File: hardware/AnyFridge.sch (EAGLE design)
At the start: 6 parts, among them U1 TSSP77038TT

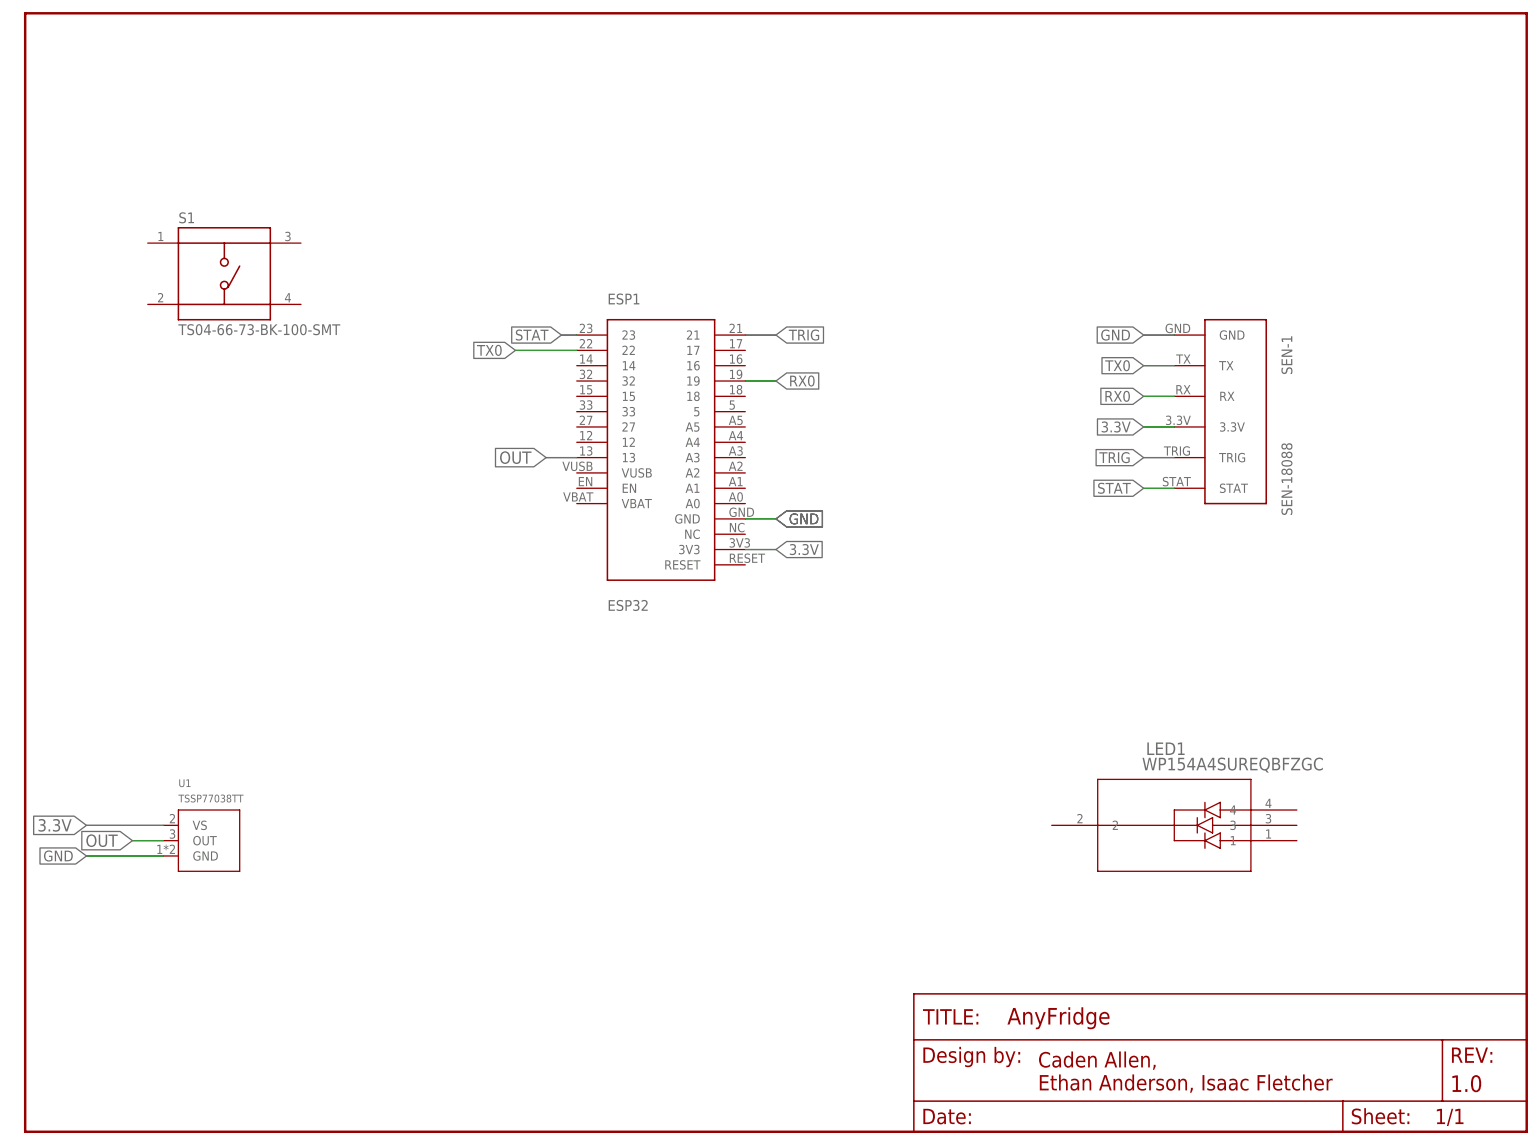
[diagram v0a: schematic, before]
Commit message: Wire LED + Button, change UART
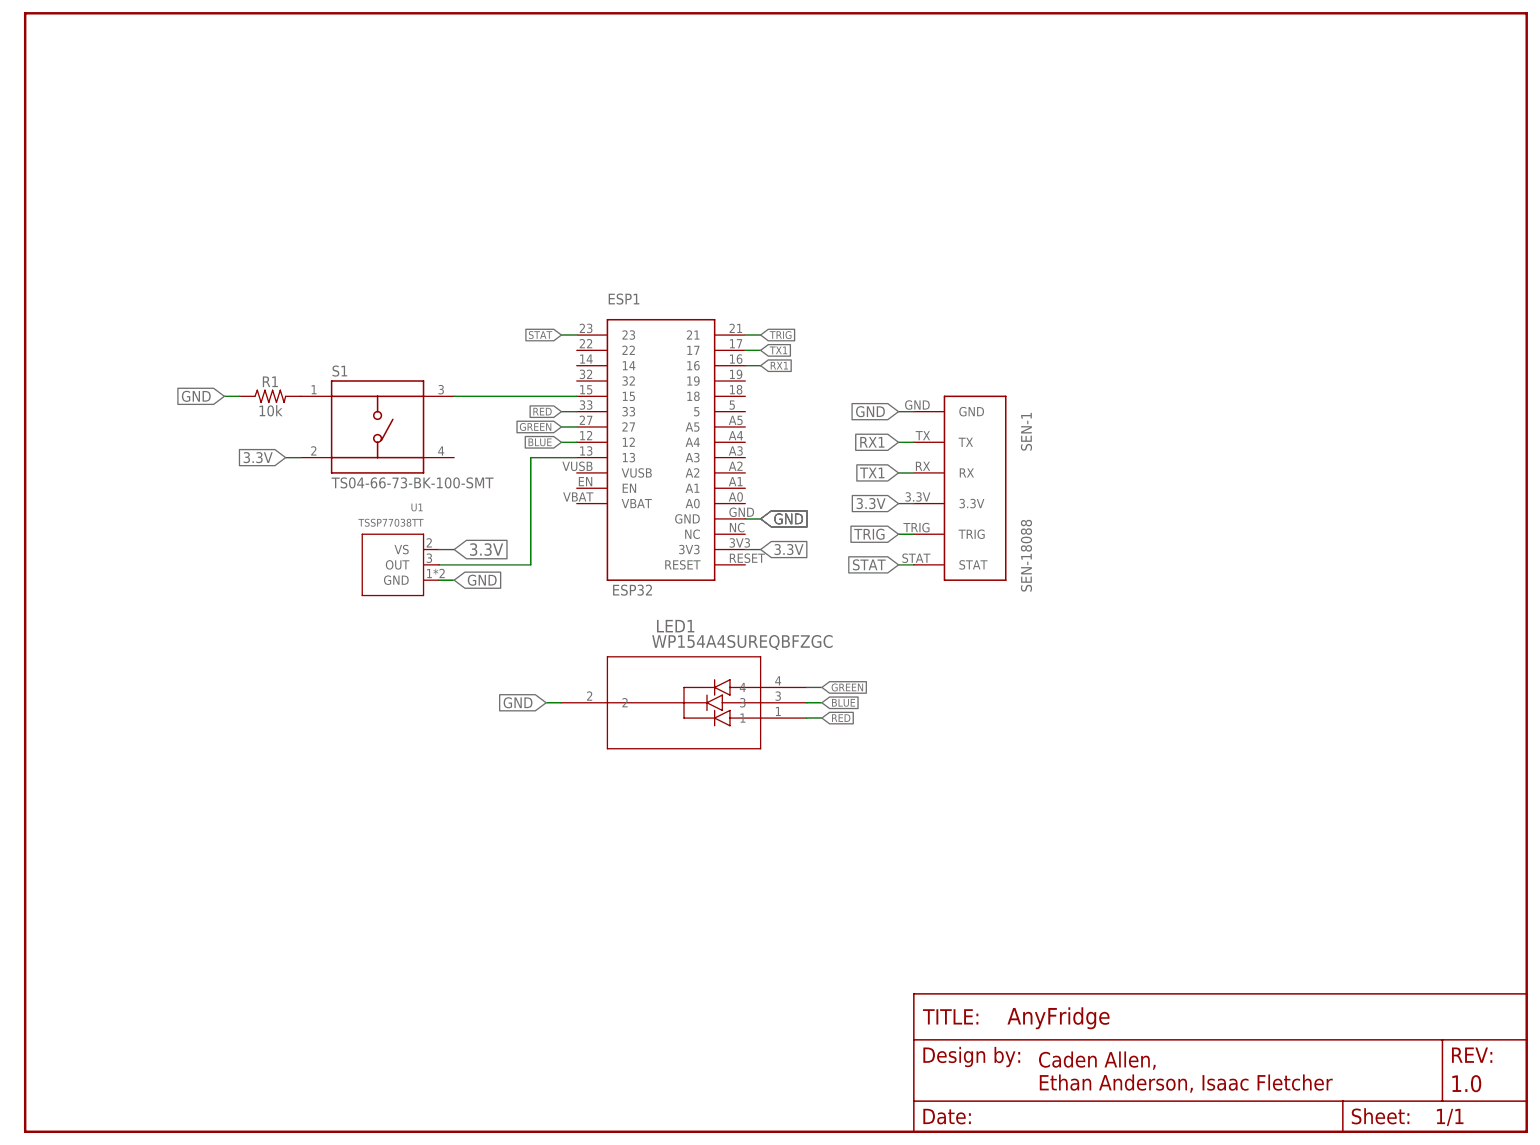
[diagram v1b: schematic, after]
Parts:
- added R1: 10k, SparkFun-Resistors:10KOHM-HORIZ-1/4W-1%
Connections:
- removed net RX0: ESP1.19, SEN-1.RX
- removed net TX0: ESP1.22, SEN-1.TX
- new net BLUE: ESP1.12, LED1.3
- new net BUTTON: ESP1.15, S1.3
- new net GREEN: ESP1.27, LED1.4
- new net N$1: R1.2, S1.1
- new net RED: ESP1.33, LED1.1
- new net RX1: ESP1.16, SEN-1.TX
- new net TX1: ESP1.17, SEN-1.RX
- net 3.3V: now also S1.2
- net GND: now also LED1.2, R1.1
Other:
- moved on the sheet: LED1, S1, SEN-1, U1

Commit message: Updated schematic
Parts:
- removed ESP1: ESP32, ESP32:ESP32
- removed LED1: WP154A4SUREQBFZGC, MISC-PARTS:WP154A4SUREQBFZGC
- removed S1: TS04-66-73-BK-100-SMT, MISC-PARTS:TS04-66-73-BK-100-SMT
- removed SEN-1: SEN-18088, SEN-18088:SEN-18088
- removed U1: TSSP77038TT, MISC-PARTS:TSSP77038TT
- added ESP: ESP32, ESP32:ESP32
- added LED: WP154A4SUREQBFZGC, MISC-PARTS:WP154A4SUREQBFZGC
- added SCANNER: SEN-18088, SEN-18088:SEN-18088
- added SENSOR: TSSP77038TT, MISC-PARTS:TSSP77038TT
- added SWITCH: TS04-66-73-BK-100-SMT, MISC-PARTS:TS04-66-73-BK-100-SMT
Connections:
- net 3.3V: now also ESP.3V3, SCANNER.3.3V, SENSOR.VS, SWITCH.2; no longer ESP1.3V3, S1.2, SEN-1.3.3V, U1.VS
- net BLUE: now also ESP.12, LED.3; no longer ESP1.12, LED1.3
- net BUTTON: now also ESP.15, SWITCH.3; no longer ESP1.15, S1.3
- net GND: now also ESP.GND, LED.2, SCANNER.GND, SENSOR.GND; no longer ESP1.GND, LED1.2, SEN-1.GND, U1.GND
- net GREEN: now also ESP.27, LED.4; no longer ESP1.27, LED1.4
- net N$1: now also SWITCH.1; no longer S1.1
- net OUT: now also ESP.13, SENSOR.OUT; no longer ESP1.13, U1.OUT
- net RED: now also ESP.33, LED.1; no longer ESP1.33, LED1.1
- net RX1: now also ESP.16, SCANNER.TX; no longer ESP1.16, SEN-1.TX
- net STAT: now also ESP.23, SCANNER.STAT; no longer ESP1.23, SEN-1.STAT
- net TRIG: now also ESP.21, SCANNER.TRIG; no longer ESP1.21, SEN-1.TRIG
- net TX1: now also ESP.17, SCANNER.RX; no longer ESP1.17, SEN-1.RX
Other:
- moved on the sheet: R1

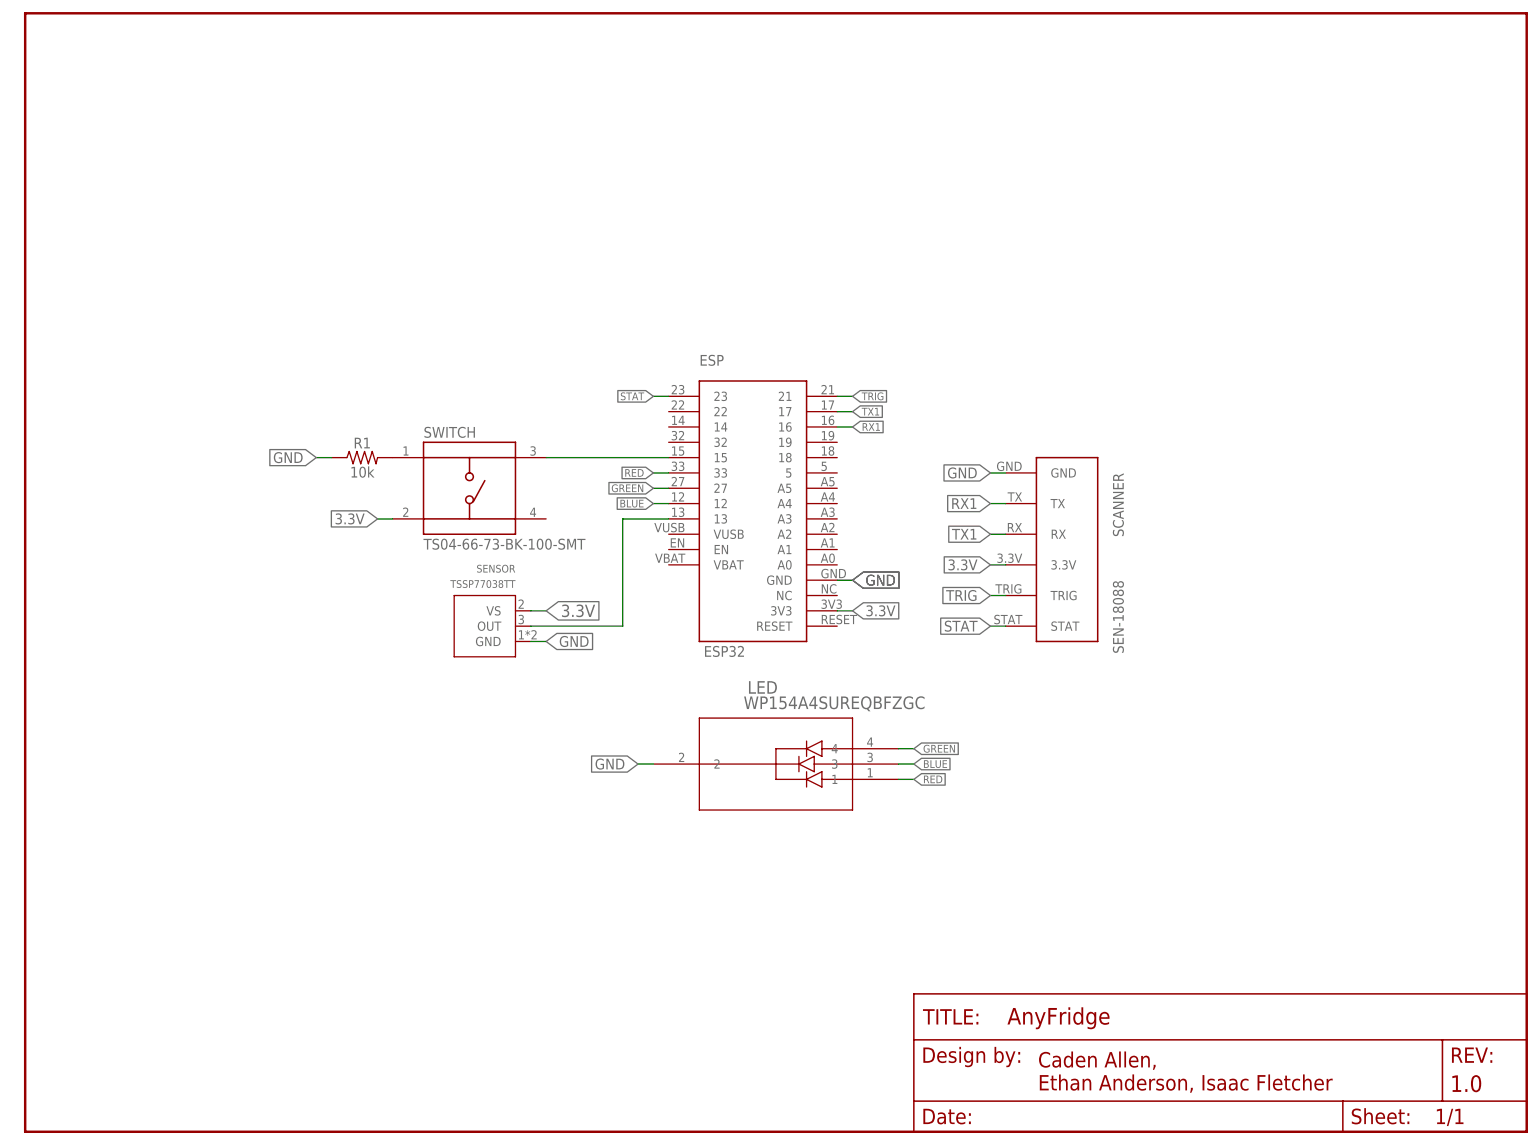
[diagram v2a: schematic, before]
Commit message: Added schematic grouping
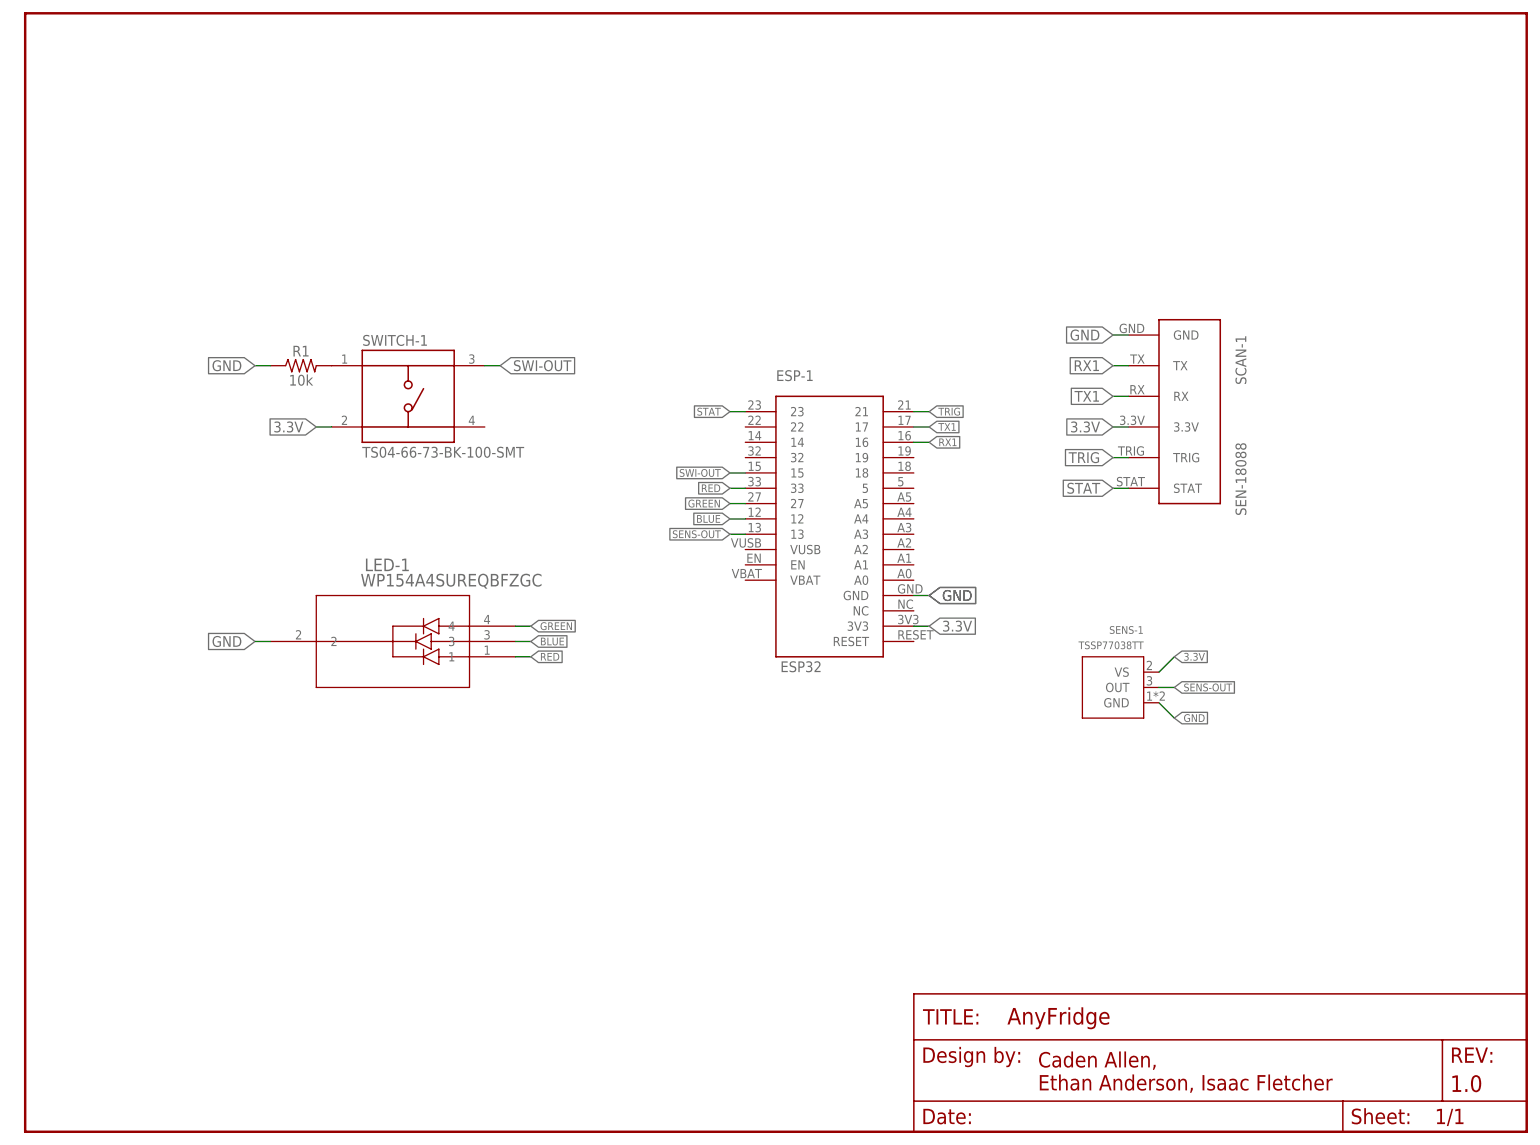
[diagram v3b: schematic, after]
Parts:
- removed ESP: ESP32, ESP32:ESP32
- removed LED: WP154A4SUREQBFZGC, MISC-PARTS:WP154A4SUREQBFZGC
- removed SCANNER: SEN-18088, SEN-18088:SEN-18088
- removed SENSOR: TSSP77038TT, MISC-PARTS:TSSP77038TT
- removed SWITCH: TS04-66-73-BK-100-SMT, MISC-PARTS:TS04-66-73-BK-100-SMT
- added ESP-1: ESP32, ESP32:ESP32
- added LED-1: WP154A4SUREQBFZGC, MISC-PARTS:WP154A4SUREQBFZGC
- added SCAN-1: SEN-18088, SEN-18088:SEN-18088
- added SENS-1: TSSP77038TT, MISC-PARTS:TSSP77038TT
- added SWITCH-1: TS04-66-73-BK-100-SMT, MISC-PARTS:TS04-66-73-BK-100-SMT
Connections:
- removed net BUTTON: ESP.15, SWITCH.3
- removed net OUT: ESP.13, SENSOR.OUT
- new net SENS-OUT: ESP-1.13, SENS-1.OUT
- new net SWI-OUT: ESP-1.15, SWITCH-1.3
- net 3.3V: now also ESP-1.3V3, SCAN-1.3.3V, SENS-1.VS, SWITCH-1.2; no longer ESP.3V3, SCANNER.3.3V, SENSOR.VS, SWITCH.2
- net BLUE: now also ESP-1.12, LED-1.3; no longer ESP.12, LED.3
- net GND: now also ESP-1.GND, LED-1.2, SCAN-1.GND, SENS-1.GND; no longer ESP.GND, LED.2, SCANNER.GND, SENSOR.GND
- net GREEN: now also ESP-1.27, LED-1.4; no longer ESP.27, LED.4
- net N$1: now also SWITCH-1.1; no longer SWITCH.1
- net RED: now also ESP-1.33, LED-1.1; no longer ESP.33, LED.1
- net RX1: now also ESP-1.16, SCAN-1.TX; no longer ESP.16, SCANNER.TX
- net STAT: now also ESP-1.23, SCAN-1.STAT; no longer ESP.23, SCANNER.STAT
- net TRIG: now also ESP-1.21, SCAN-1.TRIG; no longer ESP.21, SCANNER.TRIG
- net TX1: now also ESP-1.17, SCAN-1.RX; no longer ESP.17, SCANNER.RX
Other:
- moved on the sheet: R1
